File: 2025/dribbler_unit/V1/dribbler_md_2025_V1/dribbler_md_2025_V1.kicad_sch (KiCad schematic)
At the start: 85 parts, among them J1 Conn_01x02_Pin, J2 Conn_01x07_Pin, J3 Conn_01x02_Pin, J4 Conn_01x02_Pin, J5 Conn_01x02_Pin, J6 Conn_01x04_Pin, SW1 SW_Wuerth_450301014042, SW2 SW_Wuerth_450301014042, SW3 SW_MEC_5E, SW4 SW_Wuerth_450301014042, SW5 SW_MEC_5E, U1 MAX3051, U2 DRV8701, U3 STM32F446RETx

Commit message: PCBに紐づけ
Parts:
- removed REG1: AP7333, Package_TO_SOT_SMD:SOT-23-3, symbol dribbler_md_lib_sym:AP7333
- added REG1: LM1117GS-3.3, Package_TO_SOT_SMD:SOT-223, symbol dribbler_md_lib_sym:LM1117GS-3.3
- added Y1: CSTNE16M0V530000R0, MainBoard:OSC_CSTNE16M0V530000R0, symbol MainBoard:CSTNE16M0V530000R0
- C13: value 0.1u -> 10u
- C14: value 0.1u -> 10u; footprint Capacitor_SMD:C_0603_1608Metric_Pad1.08x0.95mm_HandSolder -> Capacitor_SMD:C_0805_2012Metric_Pad1.18x1.45mm_HandSolder
- SW1, SW2, SW4: footprint (none) -> MainBoard:slideSW
- SW3, SW5: footprint (none) -> MainBoard:SW_SKRPACE010
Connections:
- net 3.3V_sub: now also REG1.2 (VOUT)
- net GND_REG: now also REG1.3 (GND)
- net GND_log: now also Y1.2
- net at C13.1, SW2.1 (B): now also REG1.1 (VIN)
- net at U3.5 (PH0): now also Y1.1
- net at U3.6 (PH1): now also Y1.3

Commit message: 回路図完了
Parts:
- removed Y1: CSTNE16M0V530000R0, MainBoard:OSC_CSTNE16M0V530000R0, symbol MainBoard:CSTNE16M0V530000R0
- added R34: 10k, Resistor_SMD:R_0603_1608Metric_Pad0.98x0.95mm_HandSolder, symbol Device:R
- added Y1: Crystal_GND2, dribbler_md:CSTNE16M0V530000R0, symbol Device:Crystal_GND2
- J1, J3: footprint (none) -> dribbler_md:XT30
- SW1, SW2, SW4: footprint MainBoard:slideSW -> dribbler_md:IS-1235-G
- SW3, SW5: footprint MainBoard:SW_SKRPACE010 -> dribbler_md:TS-06104
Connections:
- net GND_log: now also R34.2, Y1.2; no longer R17.2, U3.20 (PA4)
- net at U3.5 (PH0): now also Y1.1
- net at U3.6 (PH1): now also Y1.3
- new net MD_SO: R17.2, R34.1, U3.20 (PA4)

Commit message: FET再選定
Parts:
- removed C2, C3: 470u, Capacitor_SMD:CP_Elec_10x10, symbol Device:C_Polarized
- removed FET1, FET2, FET3, FET4: MCMN2012A-TP, dribbler_md:MCMN2012A, symbol dribbler_md_lib_sym:MCMN2012A-TP
- removed R16: 200, Resistor_SMD:R_0603_1608Metric_Pad0.98x0.95mm_HandSolder, symbol Device:R
- removed R9: 10k, Resistor_SMD:R_0603_1608Metric_Pad0.98x0.95mm_HandSolder, symbol Device:R
- added C10, C11, C12, C13, C15, C16, C19, C2, C3, C4, C6, C7, C8, C9: 10u, Capacitor_SMD:C_0805_2012Metric_Pad1.18x1.45mm_HandSolder, symbol Device:C
- added R12, R14: 10k, Resistor_SMD:R_0402_1005Metric_Pad0.72x0.64mm_HandSolder, symbol Device:R
- added U2, U3: STS8DN3LLH5, Package_SO:SO-8_3.9x4.9mm_P1.27mm, symbol dribbler_md_lib_sym:STS8DN3LLH5
- C18: renamed from C4; value 1u -> 10u
- C5: value 1u -> 10u
- R1, R10, R13, R15, R2, R3, R4, R5, R6, R7, R8: footprint Resistor_SMD:R_0603_1608Metric_Pad0.98x0.95mm_HandSolder -> Resistor_SMD:R_0402_1005Metric_Pad0.72x0.64mm_HandSolder
- R11: value 10k -> 200; footprint Resistor_SMD:R_0603_1608Metric_Pad0.98x0.95mm_HandSolder -> Resistor_SMD:R_0402_1005Metric_Pad0.72x0.64mm_HandSolder
- R25: renamed from R24; footprint Resistor_SMD:R_0603_1608Metric_Pad0.98x0.95mm_HandSolder -> Resistor_SMD:R_0402_1005Metric_Pad0.72x0.64mm_HandSolder
- R9: renamed from R12; footprint Resistor_SMD:R_0603_1608Metric_Pad0.98x0.95mm_HandSolder -> Resistor_SMD:R_0402_1005Metric_Pad0.72x0.64mm_HandSolder
- renumbered C6 to C14, C7 to C17, C8 to C20, C9 to C21, C10 to C22, C11 to C23, C12 to C24, C13 to C25, C14 to C26, C15 to C27, C16 to C28, C17 to C29, C18 to C30, C19 to C31, C20 to C32, C21 to C33, C22 to C34, C23 to C35, C24 to C36, R14 to R16, R34 to R18, R18 to R19, R19 to R20, R20 to R21, R21 to R22, R22 to R23, R23 to R24, R25 to R26, R26 to R27, R27 to R28, R28 to R29, R29 to R30, R30 to R31, R31 to R32, R32 to R33, R33 to R34, U2 to U4, U3 to U5
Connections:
- net 18V_main: now also C10.1, C11.1, C12.1, C13.1, C15.1, C16.1, C19.1, C2.1, C3.1, C4.1, C6.1, C7.1, C8.1, C9.1, U2.7 (D1), U2.8 (D1), U3.5 (D2), U3.6 (D2)
- net GH1: now also R15.2
- net GL1: now also R13.2; no longer R15.2
- net GL2: now also R11.2; no longer R13.2
- net GND_main: now also C10.2, C11.2, C12.2, C13.2, C15.2, C16.2, C19.2, C2.2, C3.2, C4.2, C6.2, C7.2, C8.2, C9.2
- net SH1: now also R14.2, U3.3 (S2), U3.7 (D1), U3.8 (D1); no longer R11.1
- net SH2: now also R8.2, U2.1 (S1), U2.5 (D2), U2.6 (D2); no longer R8.1
- net SP: now also R10.2, R12.2, U2.3 (S2), U3.1 (S1); no longer R10.1
- net at R13.1: now also R12.1, U3.2 (G1)
- net at R15.1: now also R14.1, U3.4 (G2); no longer R10.2
- net at R9.1: now also R8.1, U2.2 (G1); no longer R8.2
- new net: R10.1, R11.1, U2.4 (G2)
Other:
- moved on the sheet: C18, C24, J1, R16, R8, R9

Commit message: FET周りを配線
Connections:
- no-connect marks 0 -> 30
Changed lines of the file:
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@@
 		(color 0 0 0 0)
+	)
+	(no_connect
+		(at 194.31 99.06)
+	)
+	(no_connect
+		(at 229.87 58.42)
+	)
+	(no_connect
+		(at 229.87 109.22)
+	)
+	(no_connect
+		(at 229.87 137.16)
+	)
+	(no_connect
+		(at 229.87 88.9)
+	)
+	(no_connect
+		(at 229.87 86.36)
+	)
+	(no_connect
+		(at 229.87 96.52)
+	)
+	(no_connect
+		(at 229.87 66.04)
+	)
+	(no_connect
+		(at 194.31 114.3)
+	)
+	(no_connect
+		(at 229.87 104.14)
+	)
+	(no_connect
+		(at 229.87 127)
+	)
+	(no_connect
+		(at 194.31 119.38)
+	)
+	(no_connect
+		(at 229.87 129.54)
+	)
+	(no_connect
+		(at 194.31 83.82)
+	)
+	(no_connect
+		(at 194.31 88.9)
+	)
+	(no_connect
+		(at 194.31 109.22)
+	)
+	(no_connect
+		(at 229.87 106.68)
+	)
+	(no_connect
+		(at 194.31 111.76)
+	)
+	(no_connect
+		(at 194.31 116.84)
+	)
+	(no_connect
+		(at 194.31 101.6)
+	)
+	(no_connect
+		(at 229.87 134.62)
+	)
+	(no_connect
+		(at 194.31 93.98)
+	)
+	(no_connect
+		(at 194.31 91.44)
+	)
+	(no_connect
+		(at 229.87 132.08)
+	)
+	(no_connect
+		(at 229.87 63.5)
+	)
+	(no_connect
+		(at 194.31 104.14)
+	)
+	(no_connect
+		(at 194.31 76.2)
+	)
+	(no_connect
+		(at 194.31 81.28)
+	)
+	(no_connect
+		(at 194.31 106.68)
+	)
+	(no_connect
+		(at 194.31 86.36)
 	)
 	(wire

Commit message: FETの配線終わり
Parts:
- C24: footprint Capacitor_SMD:C_0603_1608Metric_Pad1.08x0.95mm_HandSolder -> Capacitor_SMD:C_0805_2012Metric_Pad1.18x1.45mm_HandSolder
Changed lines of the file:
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@@
 			)
 		)
-		(property "Footprint" "Capacitor_SMD:C_0603_1608Metric_Pad1.08x0.95mm_HandSolder"
+		(property "Footprint" "Capacitor_SMD:C_0805_2012Metric_Pad1.18x1.45mm_HandSolder"
 			(at 135.5852 64.77 0)
 			(effects

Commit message: 4461周りを配線途中
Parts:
- R25: footprint Resistor_SMD:R_0402_1005Metric_Pad0.72x0.64mm_HandSolder -> Resistor_SMD:R_0603_1608Metric_Pad0.98x0.95mm_HandSolder
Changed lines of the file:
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@@
 			)
 		)
-		(property "Footprint" "Resistor_SMD:R_0402_1005Metric_Pad0.72x0.64mm_HandSolder"
+		(property "Footprint" "Resistor_SMD:R_0603_1608Metric_Pad0.98x0.95mm_HandSolder"
 			(at 311.912 41.91 90)
 			(effects

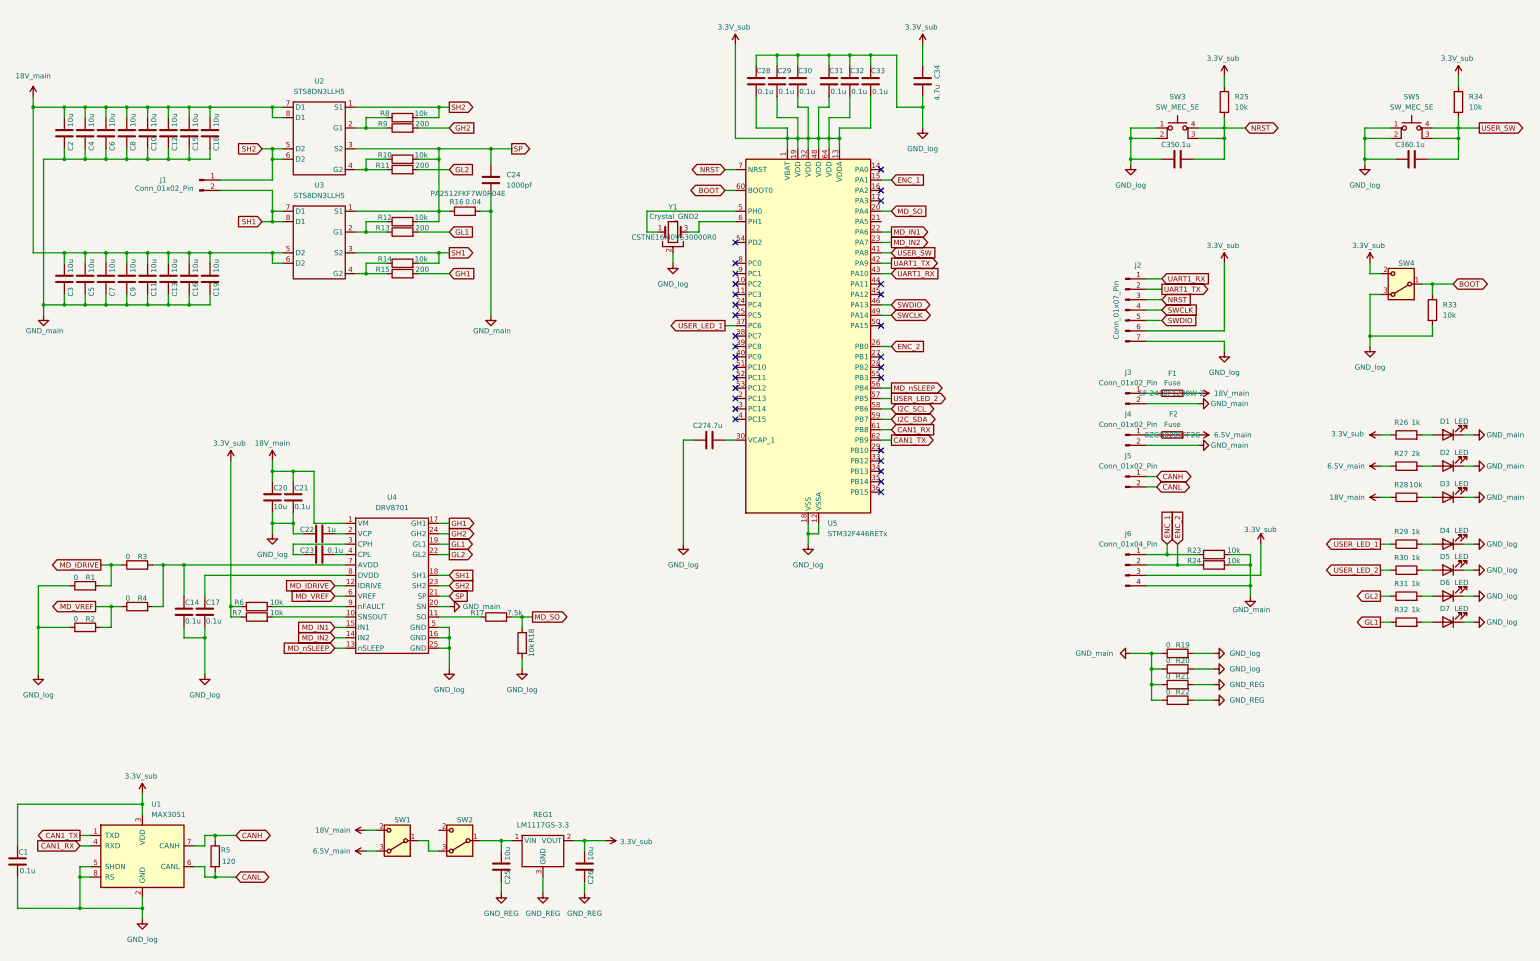
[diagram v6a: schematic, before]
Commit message: 446周りを再配線
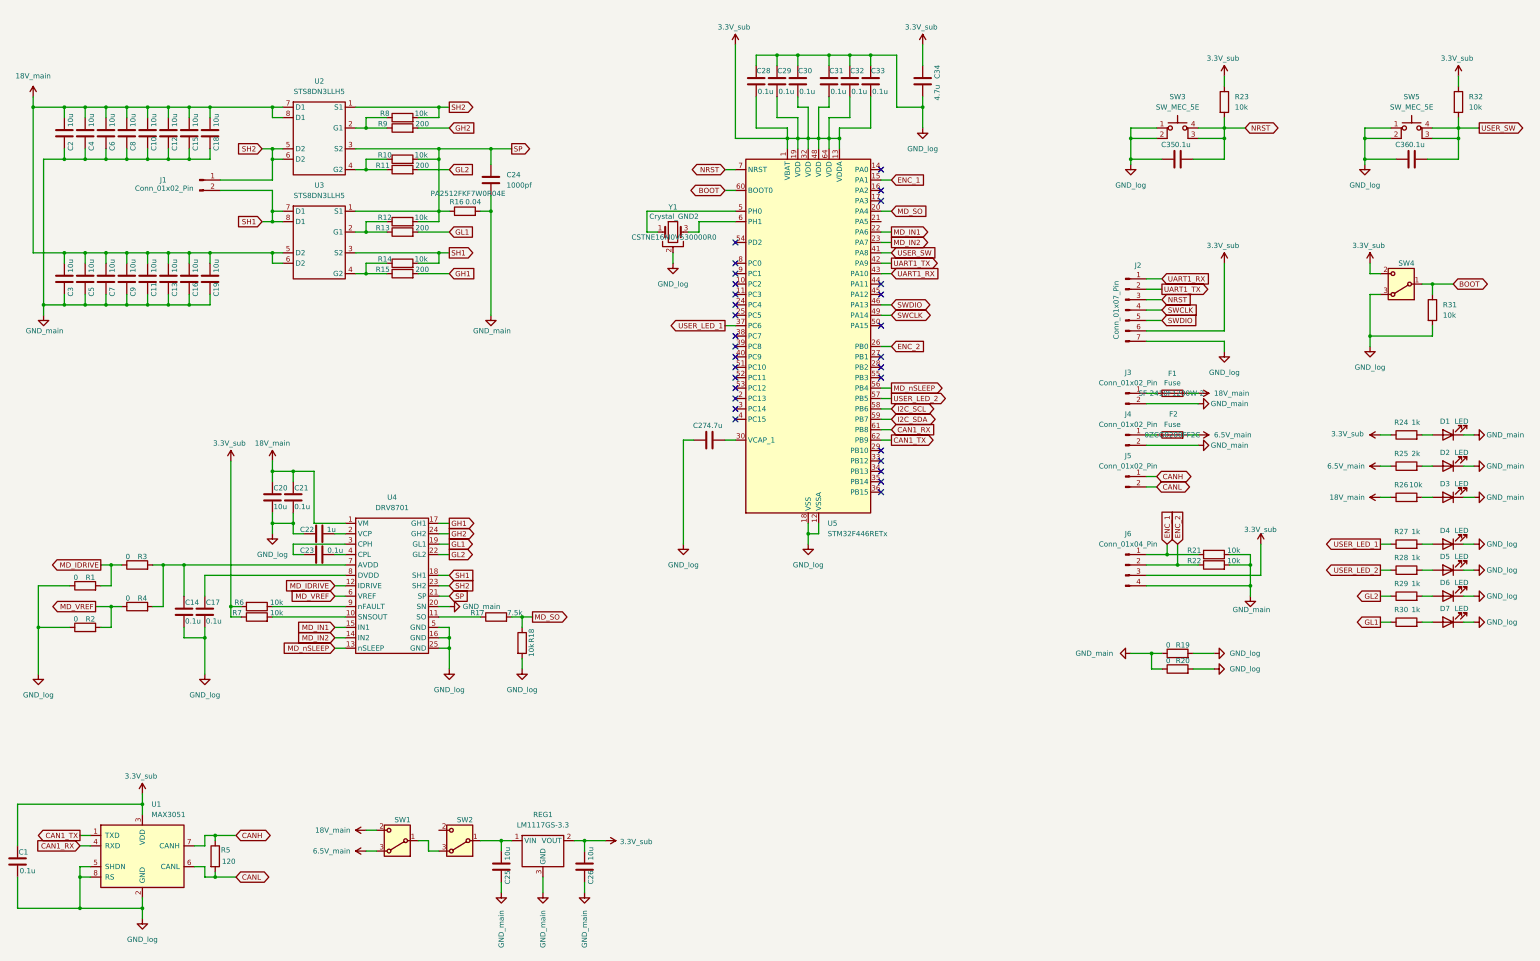
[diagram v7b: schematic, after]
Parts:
- removed R21, R22: 0, Resistor_SMD:R_0603_1608Metric_Pad0.98x0.95mm_HandSolder, symbol Device:R
- renumbered R23 to R21, R24 to R22, R25 to R23, R26 to R24, R27 to R25, R28 to R26, R29 to R27, R30 to R28, R31 to R29, R32 to R30, R33 to R31, R34 to R32
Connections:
- net GND_REG is gone; now on net GND_main: C25.2, C26.2, REG1.3 (GND)

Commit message: 配線完了
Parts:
- removed D3, D6, D7: LED, LED_SMD:LED_0603_1608Metric_Pad1.05x0.95mm_HandSolder, symbol Device:LED
- removed R26: 10k, Resistor_SMD:R_0603_1608Metric_Pad0.98x0.95mm_HandSolder, symbol Device:R
- removed R29, R30: 1k, Resistor_SMD:R_0603_1608Metric_Pad0.98x0.95mm_HandSolder, symbol Device:R
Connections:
- net GND_log: now also D1.1 (K), D2.1 (K), J6.4 (Pin_4), R21.1, R22.2
- net GND_main: no longer D1.1 (K), D2.1 (K), J6.4 (Pin_4), R21.1, R22.2
